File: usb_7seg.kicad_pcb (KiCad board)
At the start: 2 copper layers, 9 parts, among them IC1 MAX7219CNG, IC2 MAX7219CWG, U1 SeeeduinoXIAO, U2 7segment_led, U3 7segment_led

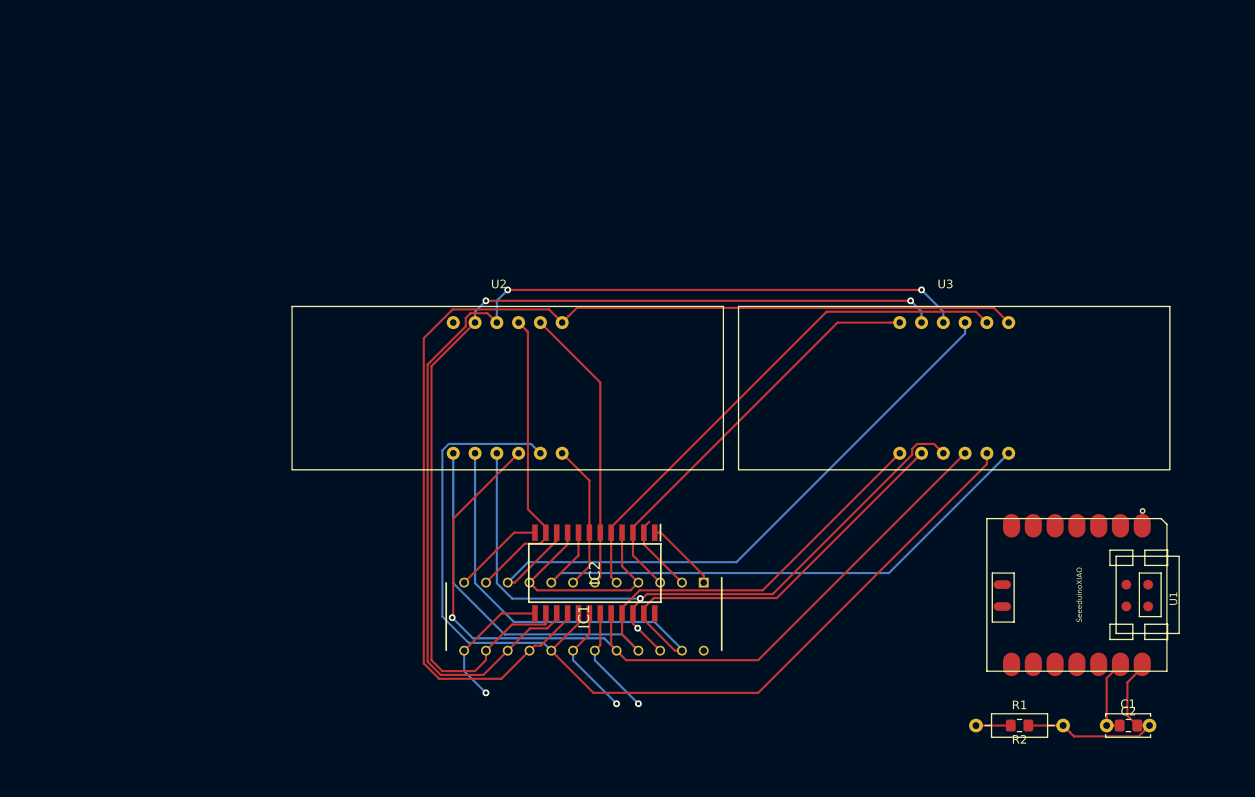
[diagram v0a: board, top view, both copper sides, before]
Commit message: 基板外形決めてDRC通してとりあえず完成
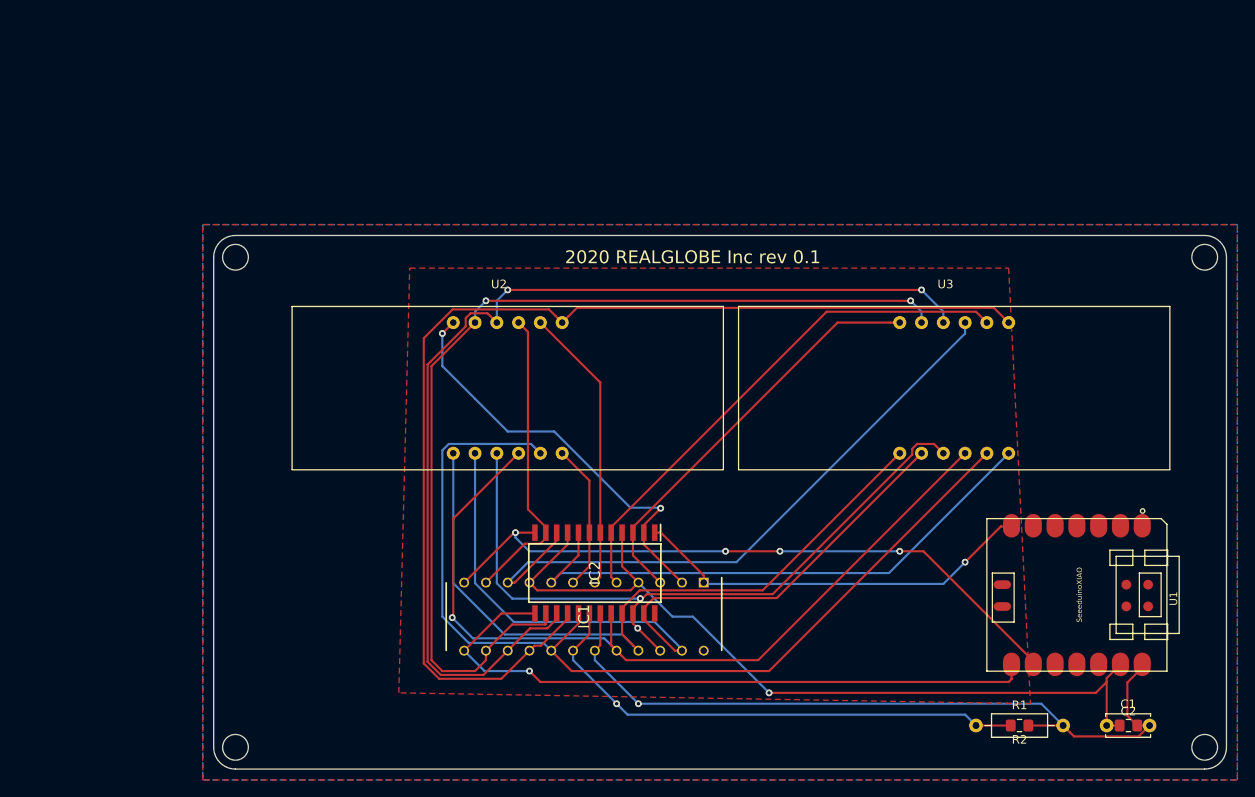
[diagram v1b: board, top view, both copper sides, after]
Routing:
- net Net-(IC1-Pad12): track 10.7 -> 78.0 mm, vias 0 -> 4
- net Net-(IC1-Pad13): track 16.0 -> 77.3 mm
- net GND: track 37.0 -> 97.5 mm, vias 0 -> 1
- net +5V: track 37.8 -> 88.4 mm
- net Net-(IC1-Pad18): track 17.5 -> 60.4 mm
- net Net-(IC1-Pad2): track 9.20 -> 49.9 mm, vias 0 -> 2
- net Net-(IC1-Pad1): track 8.61 -> 47.4 mm, vias 0 -> 1
- net Net-(IC1-Pad17): track 116.7 -> 113.9 mm
- added copper zone on F.Cu, net (none)
- added copper zone on B.Cu, net GND
- added copper zone on F.Cu, net GND
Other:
- board outline added: 118.1 x 62.2 mm
- board text added: "2020 REALGLOBE Inc rev 0.1"

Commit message: 社名入れたり、C2,R2のシルク消したり
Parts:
- renumbered C2 to ~, R2 to ~
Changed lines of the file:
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@@
     (thickness 1.6)
     (drawings 13)
-    (tracks 259)
+    (tracks 261)
     (zones 0)
     (modules 9)
@@
   (page A4)
   (layers
-    (0 F.Cu signal hide)
-    (31 B.Cu signal hide)
+    (0 F.Cu signal)
+    (31 B.Cu signal)
     (32 B.Adhes user)
     (33 F.Adhes user)
@@
     (pcbplotparams
       (layerselection 0x010fc_ffffffff)
-      (usegerberextensions false)
+      (usegerberextensions true)
       (usegerberattributes false)
       (usegerberadvancedattributes false)
@@
       (outputformat 1)
       (mirror false)
-      (drillshape 1)
+      (drillshape 0)
       (scaleselection 1)
-      (outputdirectory ""))
+      (outputdirectory "gerbers/"))
   )
   (net 0 "")
@@
     (tags "capacitor handsolder")
     (attr smd)
-    (fp_text reference C2 (at 0 -1.65) (layer F.SilkS)
+    (fp_text reference ~ (at 0 -1.65) (layer F.SilkS)
       (effects (font (size 1 1) (thickness 0.15)))
     )
@@
     (descr "24 PDIP 300mil")
     (tags "Integrated Circuit")
-    (fp_text reference IC1 (at 0 0 90) (layer F.SilkS)
+    (fp_text reference IC1 (at 3.81 17.78 90) (layer F.SilkS)
       (effects (font (size 1.27 1.27) (thickness 0.254)))
     )
@@
     (tags "Integrated Circuit")
     (attr smd)
-    (fp_text reference IC2 (at 0 0 90) (layer F.SilkS)
+    (fp_text reference IC2 (at -2.54 8.89 90) (layer F.SilkS)
       (effects (font (size 1.27 1.27) (thickness 0.254)))
     )
@@
     (tags "resistor handsolder")
     (attr smd)
-    (fp_text reference R2 (at 0 -1.65) (layer F.SilkS)
+    (fp_text reference ~ (at 0 -1.65) (layer F.SilkS)
       (effects (font (size 1 1) (thickness 0.15)))
     )
@@
       (effects (font (size 0.889 0.889) (thickness 0.1016)))
     )
-    (fp_text value SeeeduinoXIAO (at 8.89 -10.795 90) (layer F.SilkS)
+    (fp_text value SeeeduinoXIAO (at 8.89 1.27 90) (layer F.SilkS)
       (effects (font (size 0.6096 0.6096) (thickness 0.0762)))
     )
@@
   (segment (start 104.322999 50.955763) (end 104.322999 50.278239) (width 0.25) (layer F.Cu) (net 20))
   (segment (start 73.364489 67.235011) (end 88.043751 67.235011) (width 0.25) (layer F.Cu) (net 20))
-  (segment (start 71.755 68.8445) (end 73.364489 67.235011) (width 0.25) (layer F.Cu) (net 20))
   (segment (start 106.862999 49.712999) (end 107.188001 50.038001) (width 0.25) (layer F.Cu) (net 20))
   (segment (start 107.188001 50.038001) (end 107.95 50.8) (width 0.25) (layer F.Cu) (net 20))
@@
   (via (at 72.31 71.2) (size 0.8) (drill 0.4) (layers F.Cu B.Cu) (net 20))
   (segment (start 72.31 71.2) (end 71.755 70.645) (width 0.25) (layer F.Cu) (net 20))
-  (via (at 72.607059 67.747747) (size 0.8) (drill 0.4) (layers F.Cu B.Cu) (net 20))
-  (segment (start 57.678345 67.747747) (end 72.607059 67.747747) (width 0.25) (layer B.Cu) (net 20))
   (segment (start 55.88 65.949402) (end 57.678345 67.747747) (width 0.25) (layer B.Cu) (net 20))
   (segment (start 55.88 50.8) (end 55.88 65.949402) (width 0.25) (layer B.Cu) (net 20))
+  (segment (start 57.678345 67.747747) (end 72.827747 67.747747) (width 0.25) (layer B.Cu) (net 20))
+  (segment (start 72.83975 67.75975) (end 73.364489 67.235011) (width 0.25) (layer F.Cu) (net 20))
+  (via (at 72.83975 67.75975) (size 0.8) (drill 0.4) (layers F.Cu B.Cu) (net 20))
+  (segment (start 72.827747 67.747747) (end 72.83975 67.75975) (width 0.25) (layer B.Cu) (net 20))
+  (segment (start 71.755 68.8445) (end 72.83975 67.75975) (width 0.25) (layer F.Cu) (net 20))
   (segment (start 73.025 70.195243) (end 73.025 69.482) (width 0.25) (layer F.Cu) (net 21))
   (segment (start 76.649757 73.82) (end 73.025 70.195243) (width 0.25) (layer F.Cu) (net 21))

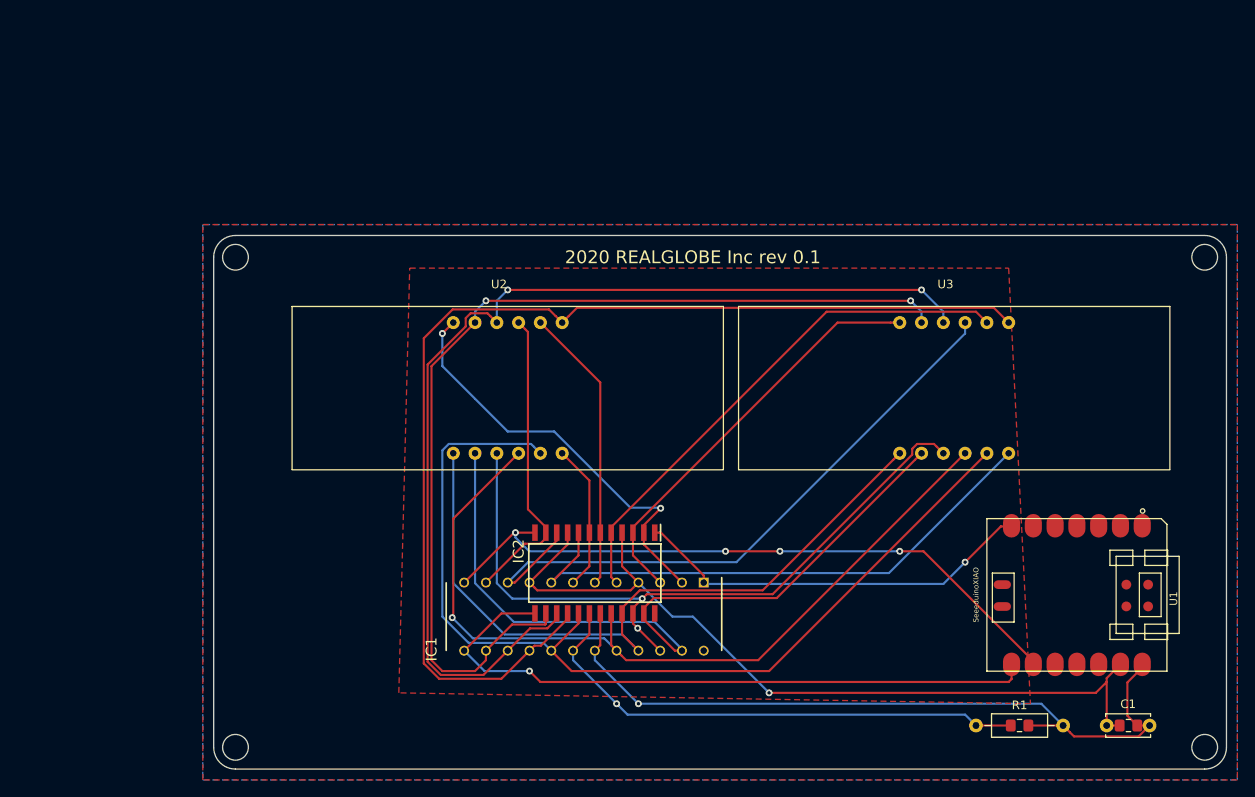
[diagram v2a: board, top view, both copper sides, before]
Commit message: 7セグLED1つ版の仮配置
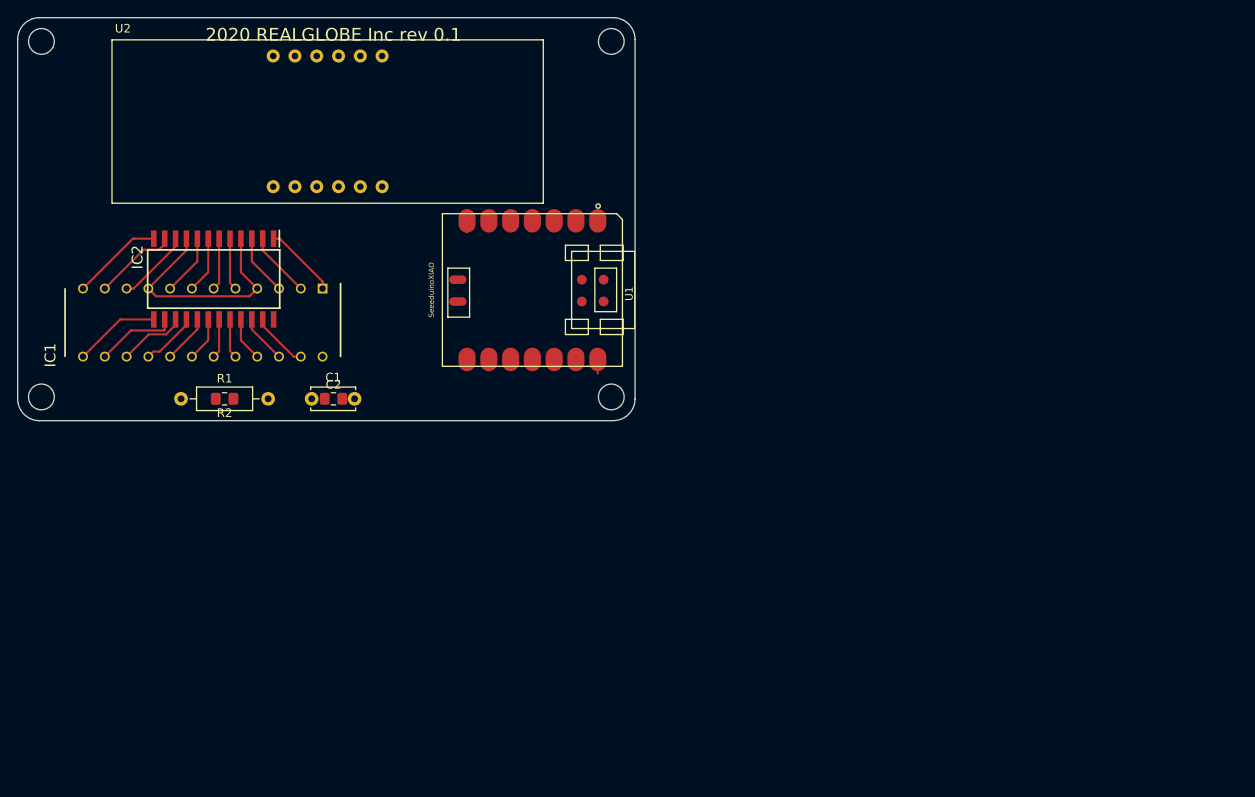
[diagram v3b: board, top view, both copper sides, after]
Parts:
- removed U3: 7segment_led, kicad_7segment_led:kicad_7segment_led_0.56
- moved C1 100.2 mm to (34.3, 44.5)
- moved R1 100.2 mm to (19.1, 44.5)
- moved R2 100.2 mm to (24.1, 44.5)
- moved C2 100.2 mm to (36.8, 44.5)
- moved U1 72.8 mm to (49.5, 22.9)
- moved IC1 56.1 mm to (21.6, 35.6)
- moved IC2 56.1 mm to (22.9, 30.5)
- moved U2 37.5 mm to (11.0, 21.6)
- renumbered ~ to C2, ~ to R2
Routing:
- net Net-(IC1-Pad16): track 130.6 -> 6.62 mm
- net Net-(IC1-Pad15): track 122.7 -> 7.89 mm, vias 2 -> 0
- net Net-(IC1-Pad17): track 113.9 -> 5.65 mm
- net Net-(IC1-Pad14): track 115.1 -> 9.49 mm, vias 2 -> 0
- net Net-(IC1-Pad20): track 98.8 -> 4.60 mm, vias 1 -> 0
- net +5V: track 88.4 -> 4.98 mm, vias 1 -> 0
- net Net-(IC1-Pad23): track 89.8 -> 7.46 mm
- net Net-(IC1-Pad21): track 85.6 -> 5.76 mm
- net Net-(IC1-Pad22): track 84.1 -> 6.29 mm, vias 2 -> 0
- net GND: track 97.5 -> 27.7 mm, vias 1 -> 0
- net Net-(IC1-Pad13): track 77.3 -> 10.1 mm, vias 1 -> 0
- net Net-(IC1-Pad12): track 78.0 -> 11.0 mm, vias 4 -> 0
- net Net-(IC1-Pad10): track 75.3 -> 8.67 mm
- net Net-(IC1-Pad8): track 66.7 -> 7.14 mm
- net Net-(IC1-Pad18): track 60.4 -> 5.13 mm, vias 1 -> 0
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- removed copper zone on F.Cu, net (none)
- removed copper zone on B.Cu, net GND
- removed copper zone on F.Cu, net GND
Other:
- board size 118.1 x 62.2 mm -> 72 x 47 mm
